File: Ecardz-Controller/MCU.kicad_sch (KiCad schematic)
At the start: 30 parts, among them J1 MEM2061-01-188-00-A, J2 Conn_01x04, J3 Conn_01x05, U1 STM32G0C1RETx

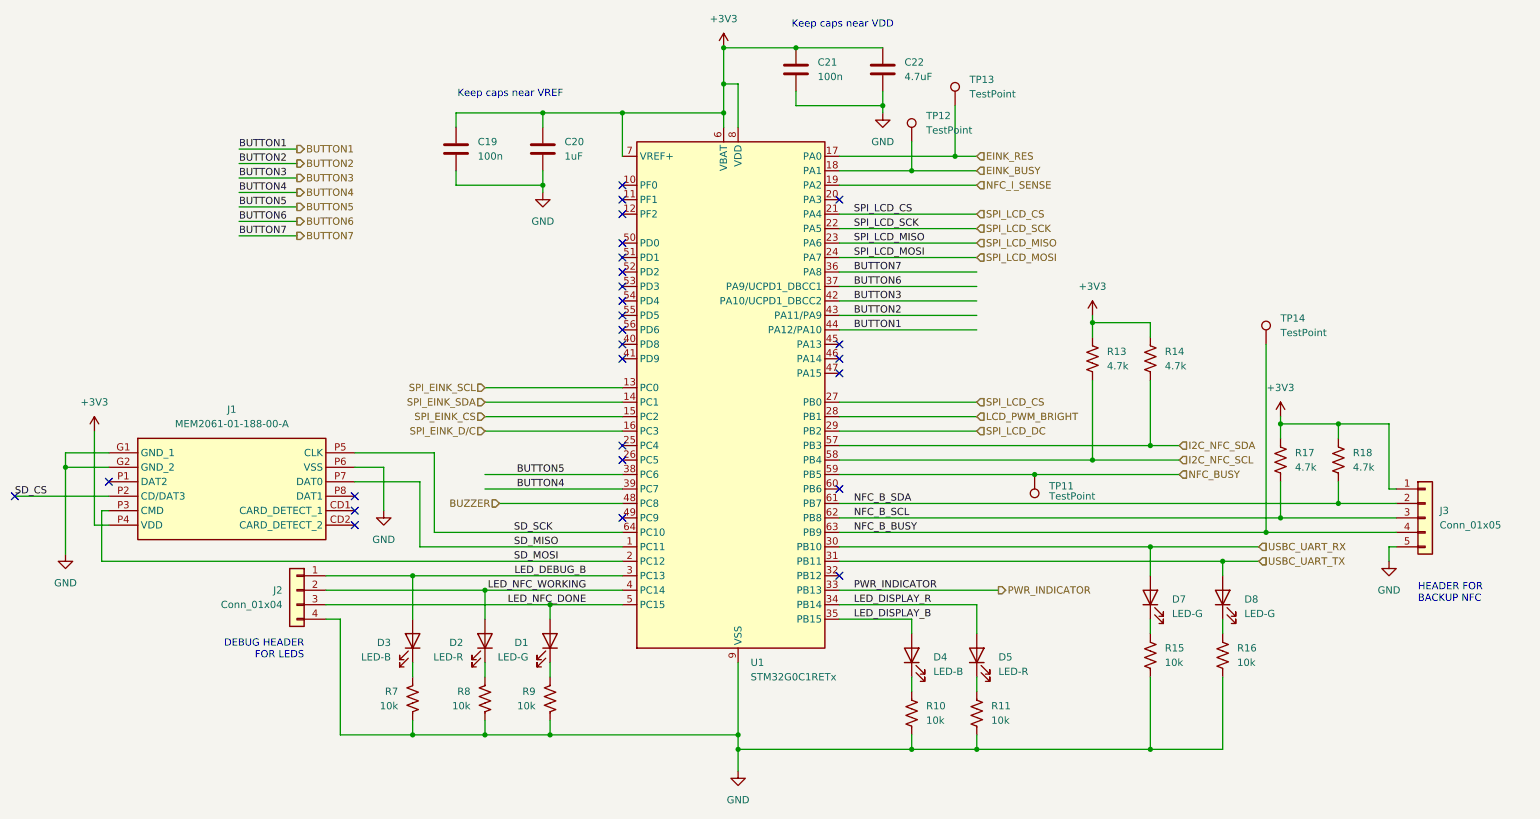
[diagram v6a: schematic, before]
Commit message: updates based on review
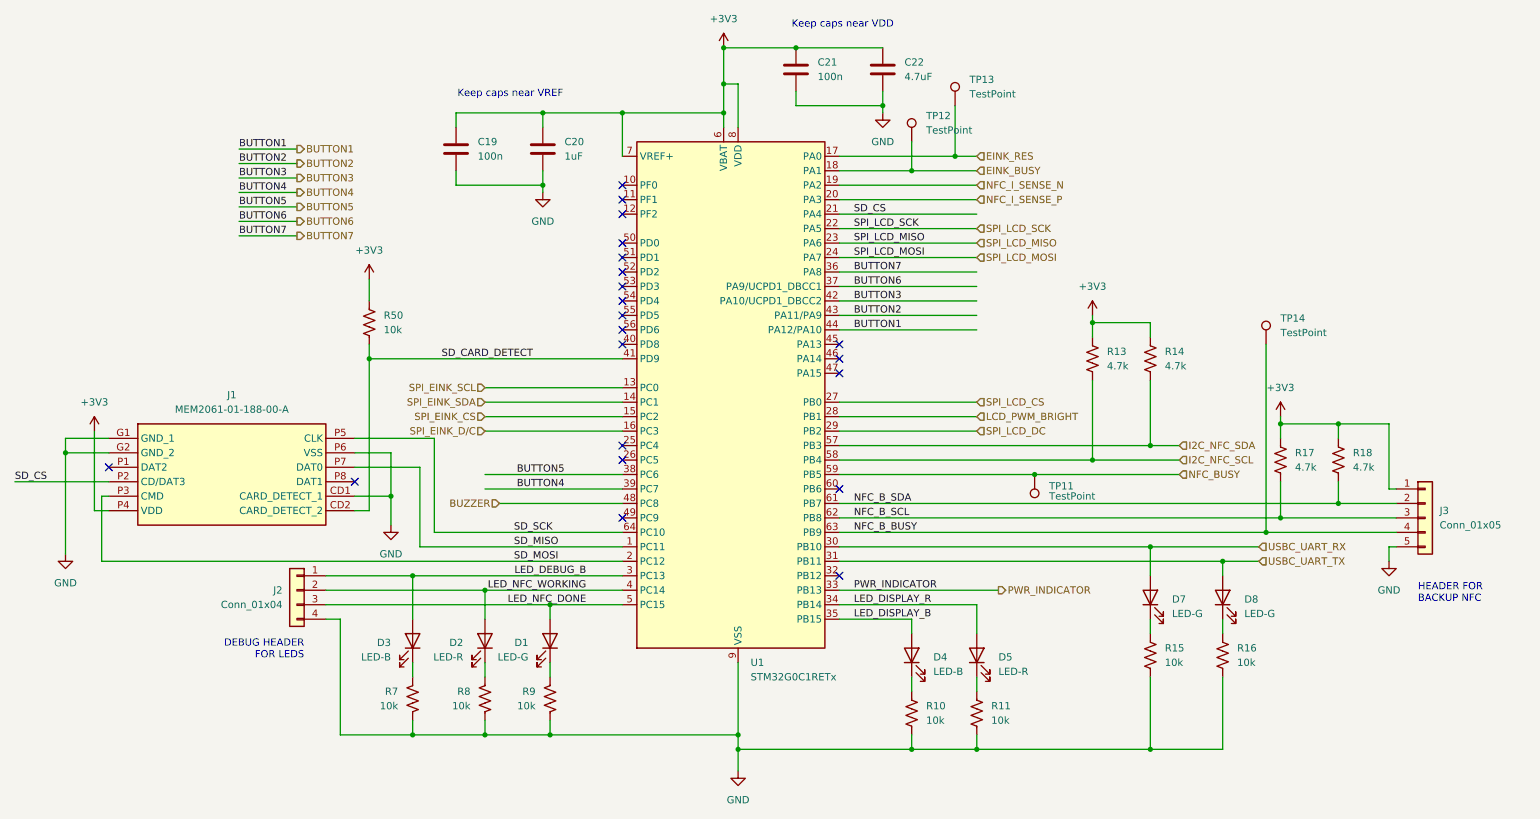
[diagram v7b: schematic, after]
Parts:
- added R50: 10k, Resistor_SMD:R_0603_1608Metric_Pad0.98x0.95mm_HandSolder, symbol Device:R_US
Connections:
- net +3V3: now also R50.1
- net GND: now also J1.CD1 (CARD_DETECT_1)
- net SD_CS: now also U1.21 (PA4)
- net SPI_LCD_CS: no longer U1.21 (PA4)
- net NFC_I_SENSE_P: now reaches U1.20 (PA3)
- net SD_CARD_DETECT: now reaches U1.41 (PD9)
- net SD_CARD_DETECT: now also J1.CD2 (CARD_DETECT_2), R50.2
- net NFC_I_SENSE renamed NFC_I_SENSE_N
- no-connect marks 26 -> 21
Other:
- moved on the sheet: J1

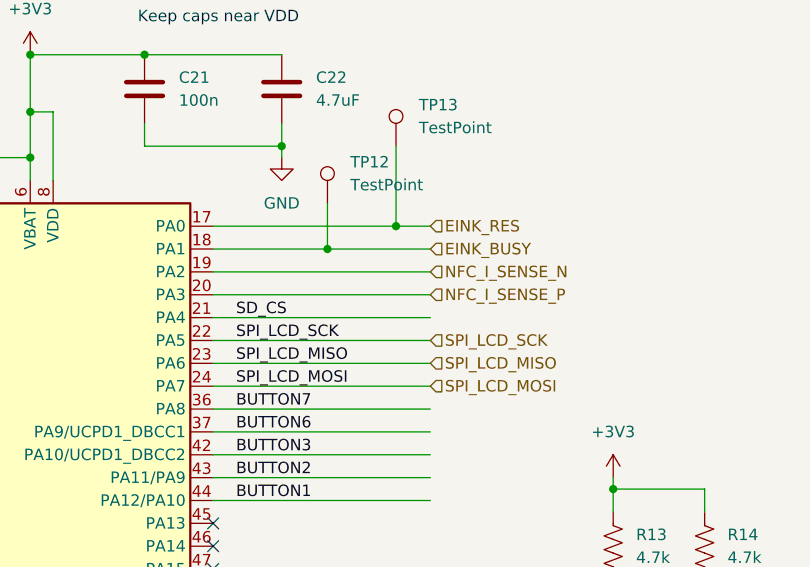
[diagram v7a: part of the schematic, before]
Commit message: added current sense resistor and modified buzzer circuit
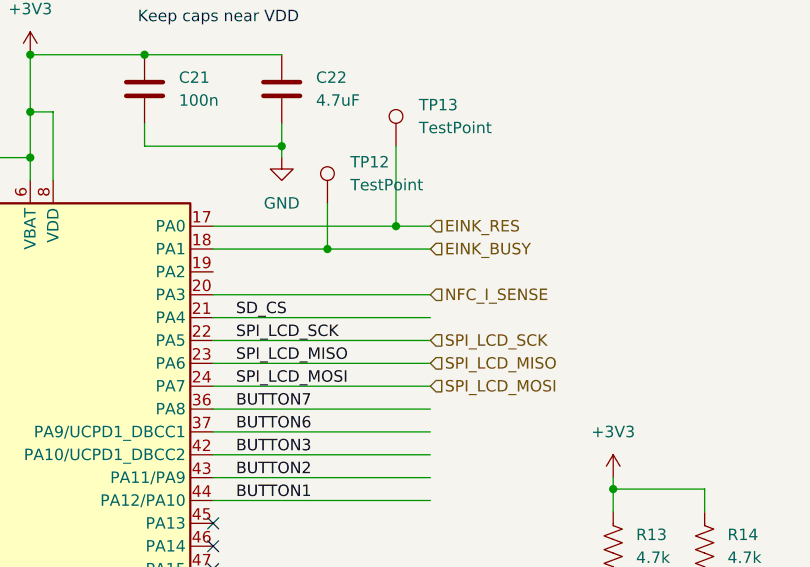
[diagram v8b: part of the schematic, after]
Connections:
- net NFC_I_SENSE_N: no longer names the net of U1.19 (PA2)
- net NFC_I_SENSE_P renamed NFC_I_SENSE
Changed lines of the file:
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@@
-	(wire
-		(pts
-			(xy 161.29 50.8) (xy 185.42 50.8)
-		)
-		(stroke
-			(width 0)
-			(type default)
-		)
-	)
 	(wire
 		(pts
@@
 		)
 	)
-	(hierarchical_label "NFC_I_SENSE_P"
+	(hierarchical_label "NFC_I_SENSE"
 		(shape input)
 		(at 185.42 53.34 0)
@@
 		(fields_autoplaced yes)
 		(effects
-			(font
-				(size 1.27 1.27)
-			)
-			(justify left)
-		)
-	)
-	(hierarchical_label "NFC_I_SENSE_N"
-		(shape input)
-		(at 185.42 50.8 0)
-		(fields_autoplaced yes)
-		(effects
